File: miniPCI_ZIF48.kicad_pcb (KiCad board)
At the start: 2 copper layers, 59.6 x 50.9 mm, 6 parts

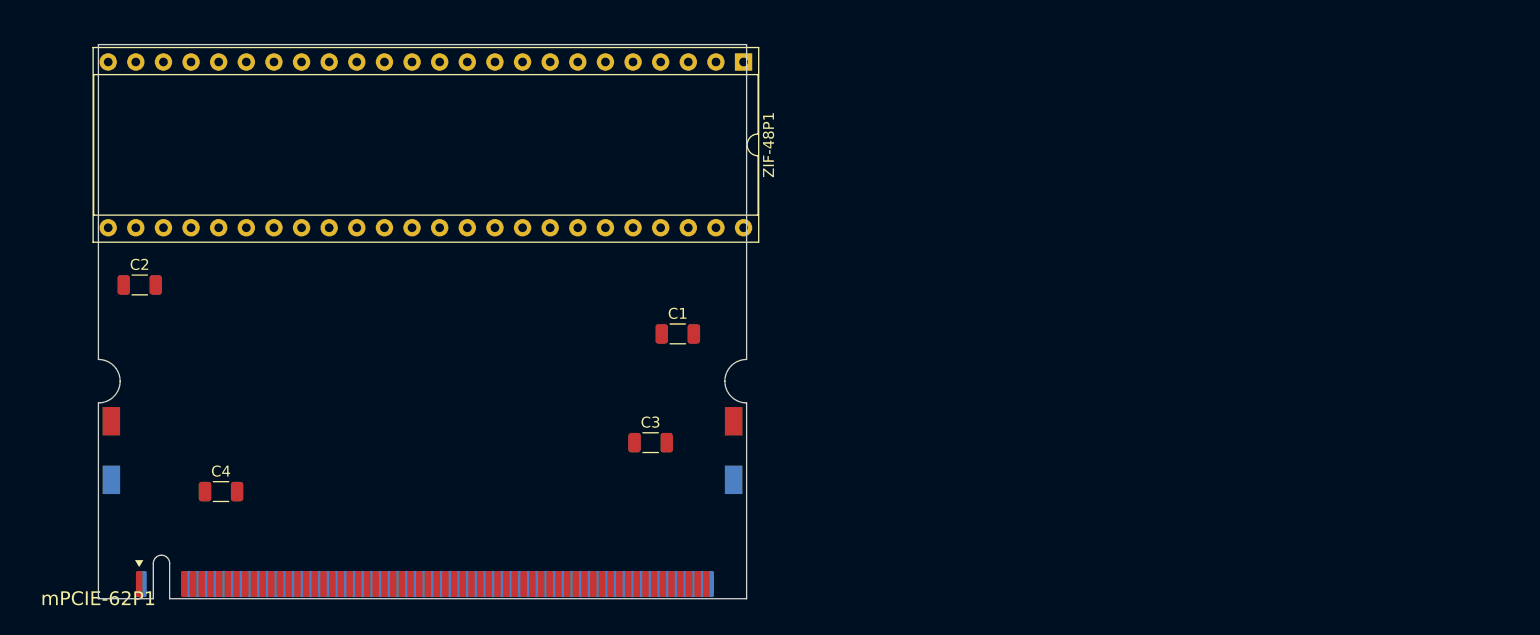
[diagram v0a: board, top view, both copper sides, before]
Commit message: re-mapping mPCIe -> same 62 pins on both side.
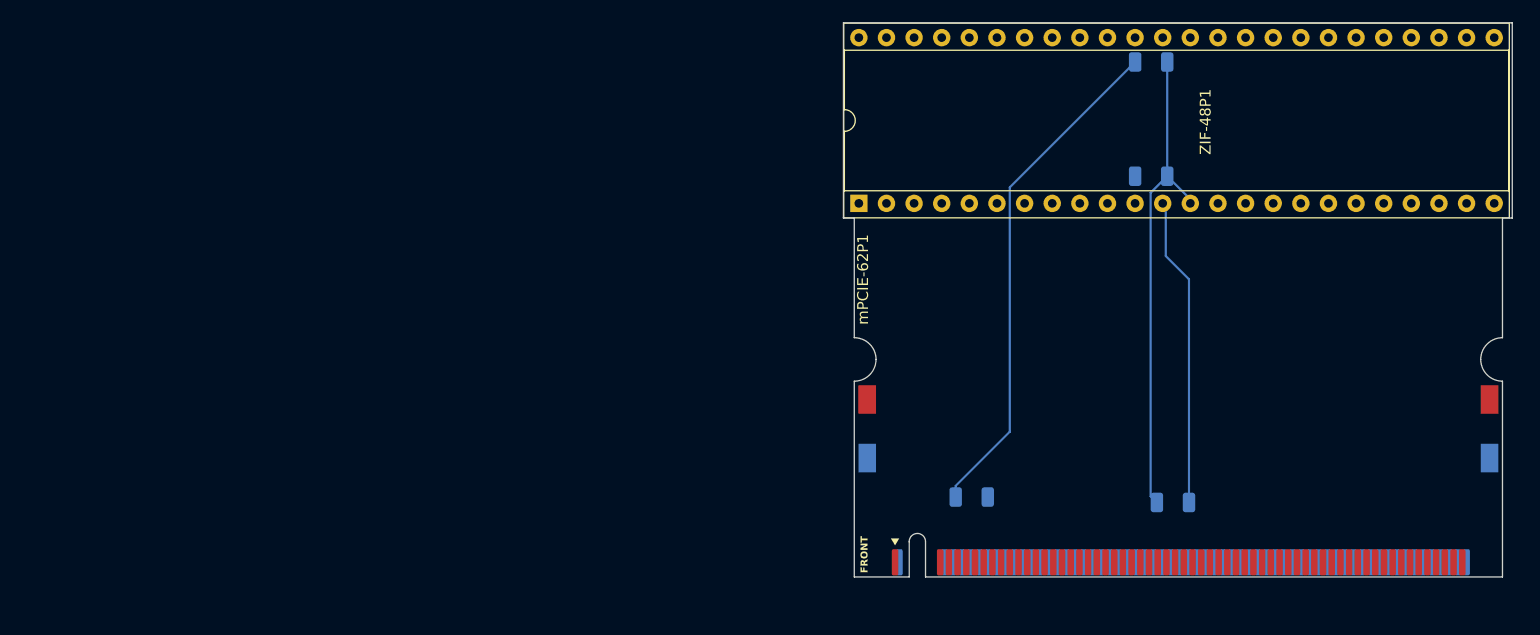
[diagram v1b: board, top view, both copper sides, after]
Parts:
- C1, C2, C3, C4: moved to B.Cu
- moved C2 97.1 mm to (164.5, 133.0)
- moved C4 94.2 mm to (162.5, 92.5)
- moved mPCIE-62P1 69.5 mm to (135.2, 139.8)
- moved C1 45.9 mm to (162.5, 103.0)
- moved C3 29.9 mm to (146.0, 132.5), turned to 180 degrees
- moved ZIF-48P1 16.8 mm to (135.6, 105.5), turned to 90 degrees
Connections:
- mPCIE-62P1 pad 10: unconnected-(mPCIE-62P1-NO-Pad10) -> GND
- mPCIE-62P1 pad 11: unconnected-(mPCIE-62P1-CE4-Pad11) -> unconnected-(ZIF-48P1-Pad11)
- mPCIE-62P1 pad 2: unconnected-(mPCIE-62P1-3.3V-Pad2) -> unconnected-(ZIF-48P1-Pad2)
- mPCIE-62P1 pad 3: unconnected-(mPCIE-62P1-VCC-Pad3) -> unconnected-(ZIF-48P1-Pad3)
- mPCIE-62P1 pad 4: unconnected-(mPCIE-62P1-VEXT-Pad4) -> unconnected-(ZIF-48P1-Pad4)
- mPCIE-62P1 pad 7: unconnected-(mPCIE-62P1-NO-Pad7) -> (no net)
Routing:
- net V2-5: track 0.00 -> 46.8 mm
- net GND: track 0.00 -> 44.8 mm
- net V2-58: track 0.00 -> 28.4 mm
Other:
- board size 59.6 x 50.9 mm -> 61.5 x 50.9 mm
- board text added: "BACK"
- board text added: "FRONT"

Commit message: Passed all DRCs/PCB_Editor
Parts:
- C1, C2, C3, C4: footprint Capacitor_SMD:C_1206_3216Metric -> Capacitor_THT:C_Axial_L3.8mm_D2.6mm_P7.50mm_Horizontal
- moved ZIF-48P1 60.3 mm to (194.0, 90.5), turned to -90 degrees
- moved C2 27.2 mm to (189.0, 121.2), turned to -90 degrees
- moved C1 8.84 mm to (166.2, 95.0)
- moved C4 8.84 mm to (166.2, 100.5)
- moved C3 6.25 mm to (147.8, 126.5)
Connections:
- mPCIE-62P1 pad 10: GND -> unconnected-(mPCIE-62P1-NO-Pad10)_1
- mPCIE-62P1 pad 11: unconnected-(ZIF-48P1-Pad11) -> unconnected-(mPCIE-62P1-CE4-Pad11)_1
- mPCIE-62P1 pad 2: unconnected-(ZIF-48P1-Pad2) -> unconnected-(mPCIE-62P1-3.3V-Pad2)
- mPCIE-62P1 pad 3: unconnected-(ZIF-48P1-Pad3) -> unconnected-(mPCIE-62P1-VCC-Pad3)_1
- mPCIE-62P1 pad 4: unconnected-(ZIF-48P1-Pad4) -> unconnected-(mPCIE-62P1-VEXT-Pad4)
- mPCIE-62P1 pad 7: (no net) -> unconnected-(mPCIE-62P1-NO-Pad7)
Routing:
- net GND: track 44.8 -> 269.1 mm, vias 0 -> 19
- net ALE: track 0.00 -> 61.6 mm, vias 0 -> 1
- net WE: track 0.00 -> 60.6 mm, vias 0 -> 1
- net V2-58: track 28.4 -> 88.9 mm, vias 0 -> 2
- net CLE: track 0.00 -> 60.1 mm, vias 0 -> 2
- net CE3: track 0.00 -> 57.8 mm, vias 0 -> 1
- net CE2: track 0.00 -> 57.6 mm, vias 0 -> 2
- net RB1: track 0.00 -> 55.7 mm, vias 0 -> 1
- net RE: track 0.00 -> 54.9 mm, vias 0 -> 2
- net CE0: track 0.00 -> 54.5 mm, vias 0 -> 1
- net RB2: track 0.00 -> 54.4 mm, vias 0 -> 1
- net CE1: track 0.00 -> 51.3 mm, vias 0 -> 2
- net D9: track 0.00 -> 46.1 mm, vias 0 -> 2
- net D0: track 0.00 -> 45.9 mm, vias 0 -> 1
- net D1: track 0.00 -> 45.1 mm, vias 0 -> 1
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- added copper zone on In2.Cu, net GND
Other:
- board size 61.5 x 50.9 mm -> 62.5 x 51 mm
- copper layers 2 -> 4

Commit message: Add Texts & Design
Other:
- board text added: "@Radovan Hlaváček @Nguyễn Vũ Hà @deulamco"
- board text added: "Aug, 8th 2024 miniPCI_ZIF48 rev.1"
- board text added: "DRC LAB"
- board text added: "KiCAD"
- board text added: "Made in VietNam."
- board text added: "Made with"
- board text added: "MiniPCI to ZIF48"

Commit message: Silkscreen design & finish Gerber.
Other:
- board text added: "MiniPCI To ZIF48"
- board text removed: "@Radovan Hlaváček @Nguyễn Vũ Hà @deulamco"
- board text removed: "MiniPCI to ZIF48"
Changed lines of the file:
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@@
 		(allow_soldermask_bridges_in_footprints no)
 		(pcbplotparams
-			(layerselection 0x00010fc_ffffffff)
+			(layerselection 0x00011fc_ffffffff)
 			(plot_on_all_layers_selection 0x0000000_00000000)
 			(disableapertmacros no)
@@
 			(outputformat 1)
 			(mirror no)
-			(drillshape 1)
+			(drillshape 0)
 			(scaleselection 1)
-			(outputdirectory "")
+			(outputdirectory "../../../Downloads/mPCI_ZIF48/")
 		)
 	)
@@
 		(descr "Footprint is based on the official http://read.pudn.com/downloads61/doc/210851/MiniPCI.pdf Mini PCI Specification (Revision 1.0 October 25, 1999).\nPage: 53..61 (Mechanical Design Details)")
 		(property "Reference" "mPCIE-62P1"
-			(at 1.3 -27.35 270)
+			(at 1.3 -27.35 -90)
 			(layer "B.SilkS")
 			(effects
@@
 		(tags "C Axial series Axial Horizontal pin pitch 7.5mm  length 3.8mm diameter 2.6mm")
 		(property "Reference" "C1"
-			(at 3.75 2.42 360)
+			(at 3.75 2.42 0)
 			(layer "B.SilkS")
 			(effects
@@
 		)
 		(property "Value" "100NF"
-			(at 3.75 -2.42 360)
+			(at 3.75 -2.42 0)
 			(layer "B.Fab")
 			(effects
@@
 		)
 		(fp_text user "${REFERENCE}"
-			(at 3.75 0 360)
+			(at 3.75 0 0)
 			(layer "B.Fab")
 			(effects
@@
 		)
 	)
-	(gr_text "@Radovan Hlaváček\n@Nguyễn Vũ Hà\n@deulamco"
-		(at 135.5 113 0)
-		(layer "F.SilkS")
-		(effects
-			(font
-				(size 0.65 0.65)
-				(thickness 0.1)
-			)
-			(justify left bottom)
-		)
-	)
 	(gr_text "DRC LAB"
 		(at 156.5 112 0)
@@
 		)
 	)
-	(gr_text "MiniPCI to ZIF48\n"
-		(at 135.5 109.5 0)
+	(gr_text "MiniPCI To ZIF48\n"
+		(at 142.5 109.5 0)
 		(layer "F.SilkS")
 		(effects
@@
 				(bold yes)
 			)
-			(justify left bottom)
+			(justify bottom)
 		)
 	)

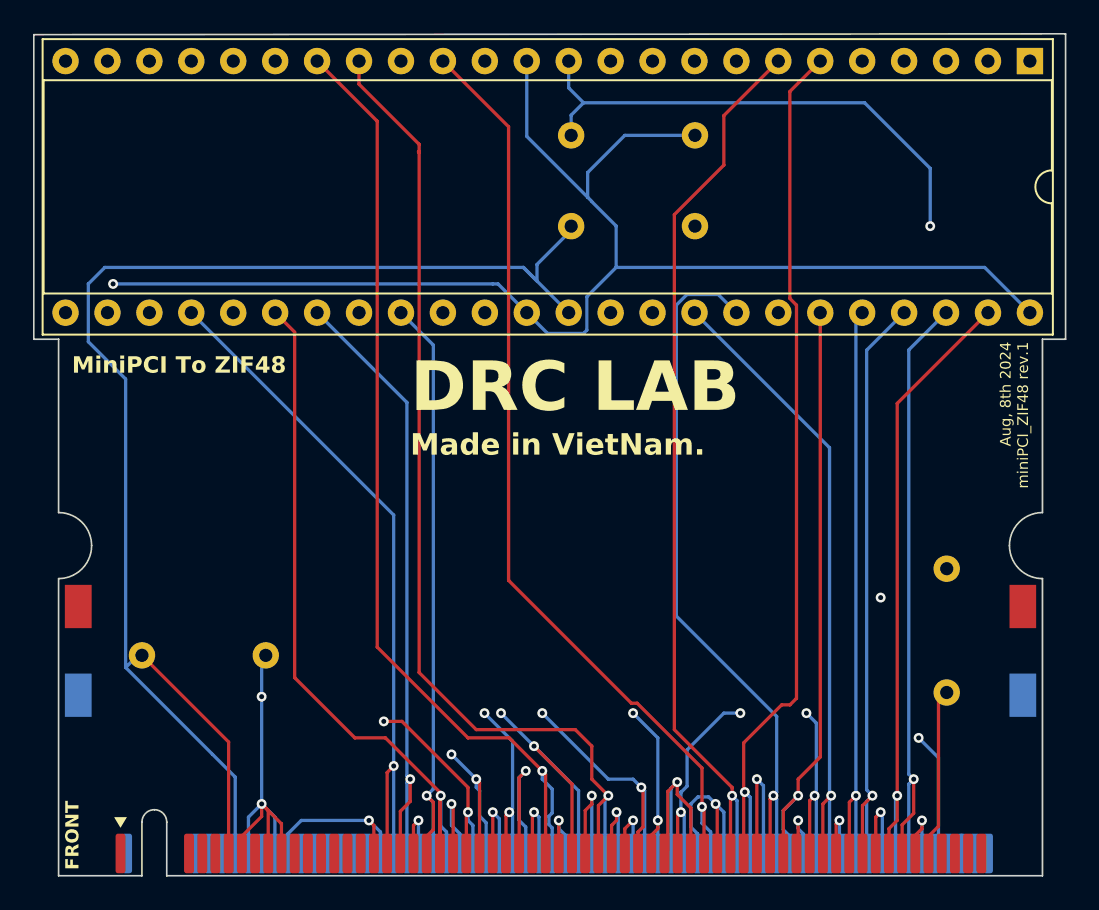
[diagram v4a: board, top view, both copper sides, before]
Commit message: Refine into only 2-layers design, both copper filled.
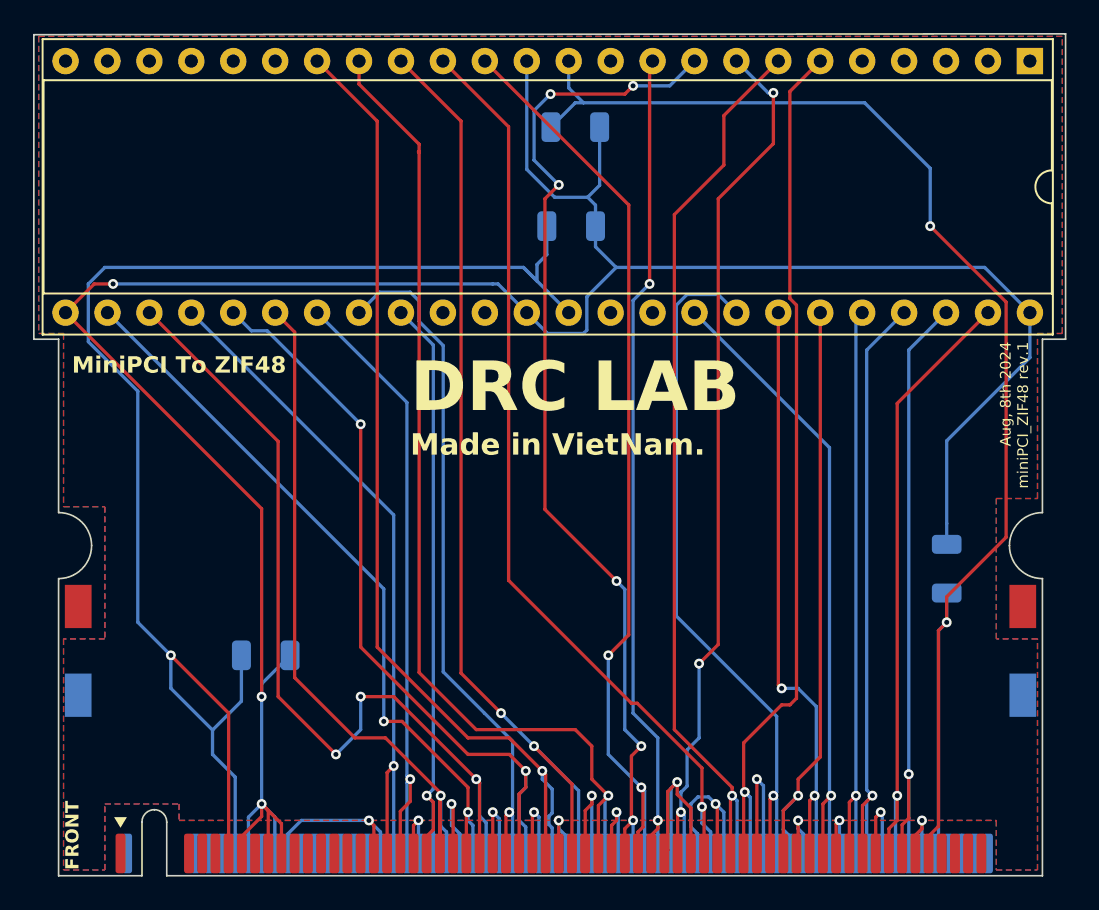
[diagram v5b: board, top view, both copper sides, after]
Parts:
- C1, C2, C3, C4: footprint Capacitor_THT:C_Axial_L3.8mm_D2.6mm_P7.50mm_Horizontal -> Capacitor_SMD:C_1206_3216Metric
- moved C1 0.56 mm to (166.5, 94.5)
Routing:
- net GND: track 269.1 -> 256.2 mm, vias 19 -> 18
- net D9: track 46.1 -> 54.0 mm, vias 2 -> 3
- net CE0: track 54.5 -> 61.9 mm, vias 1 -> 6
- net D3: track 39.4 -> 42.9 mm, vias 2 -> 1
- net V2-5: track 90.0 -> 92.6 mm, vias 0 -> 1
- net D0: track 45.9 -> 47.6 mm, vias 1 -> 2
- net RE: track 54.9 -> 54.1 mm, vias 2 -> 3
- net V2-58: track 88.9 -> 89.7 mm
- added copper zone on B.Cu, net (none)
- added copper zone on F.Cu, net (none)
- removed copper zone on In2.Cu, net GND
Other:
- copper layers 4 -> 2
